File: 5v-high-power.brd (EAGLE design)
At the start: 92.7 x 34.6 mm, 31 parts, among them IC1 LM2576, J1 Bypass, J2 En, J3 12v, J4 5V Out, J5 LEN EN, J6 POWERPOLE_POWER25A, J7 POWERPOLE_POWER25A, Q1 SI4532ADY

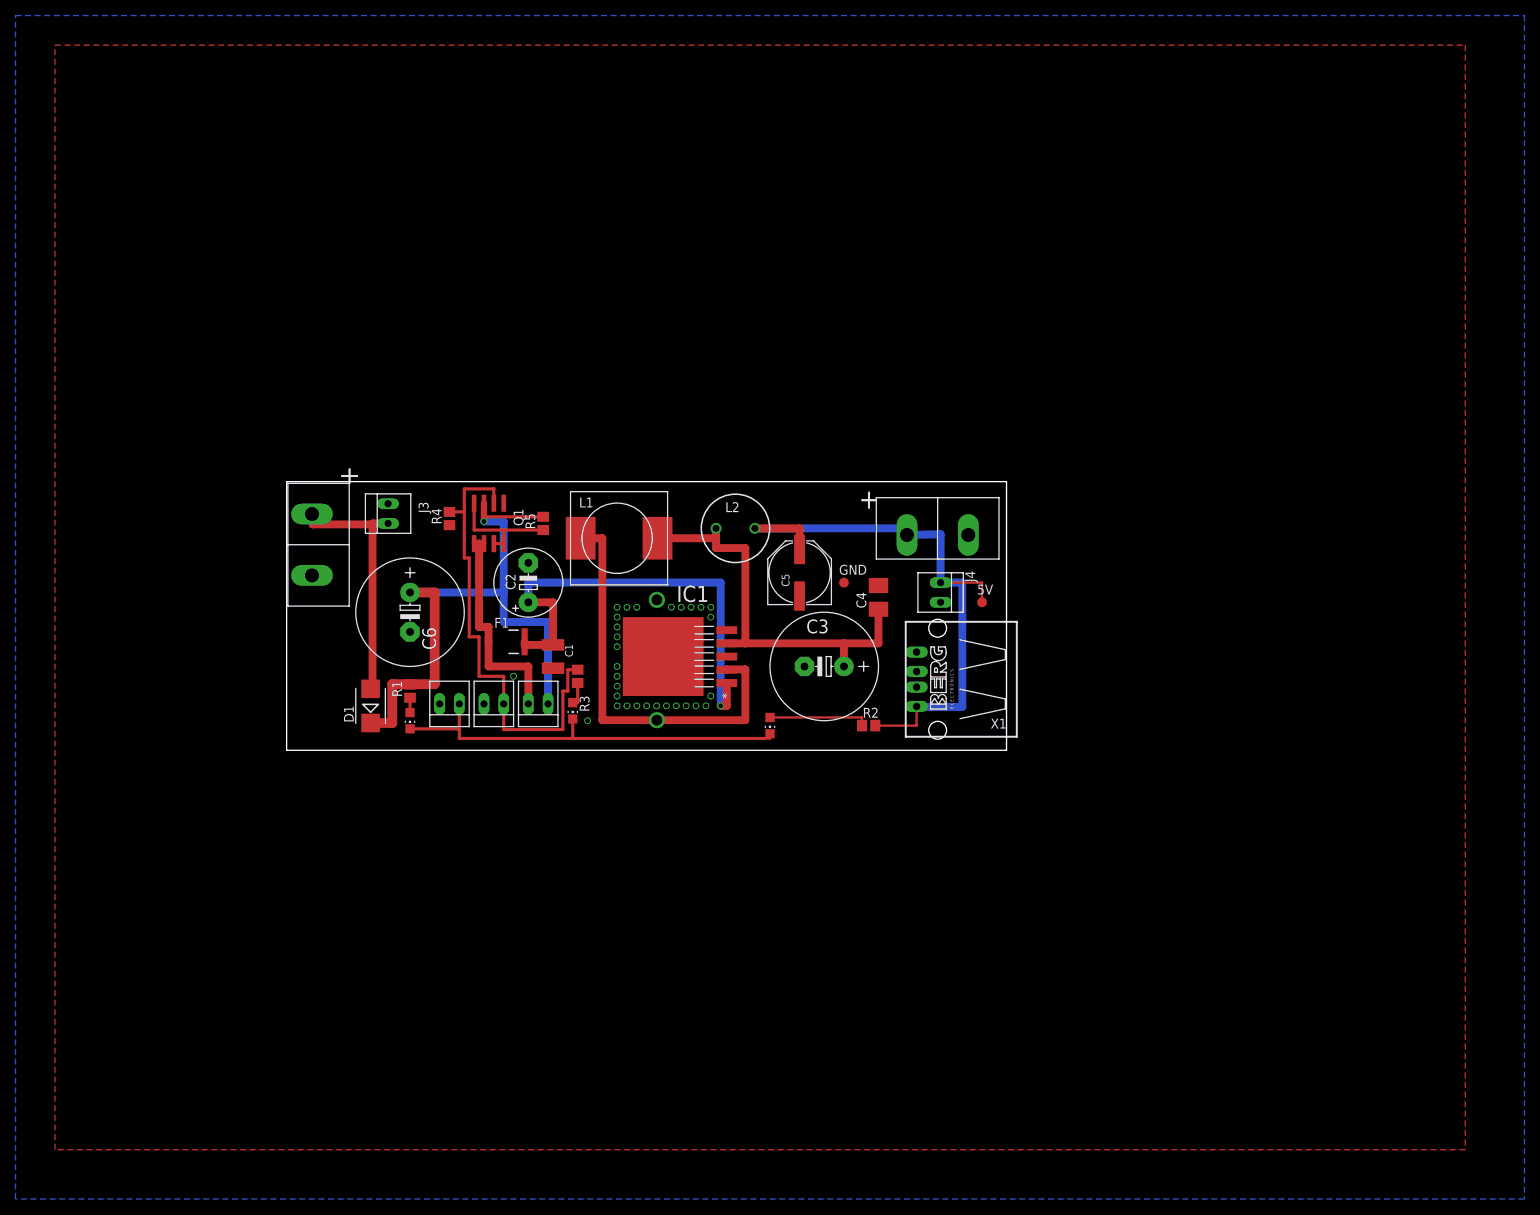
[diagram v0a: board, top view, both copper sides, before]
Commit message: uses a4 frame and smaller ground plane area to make printing better
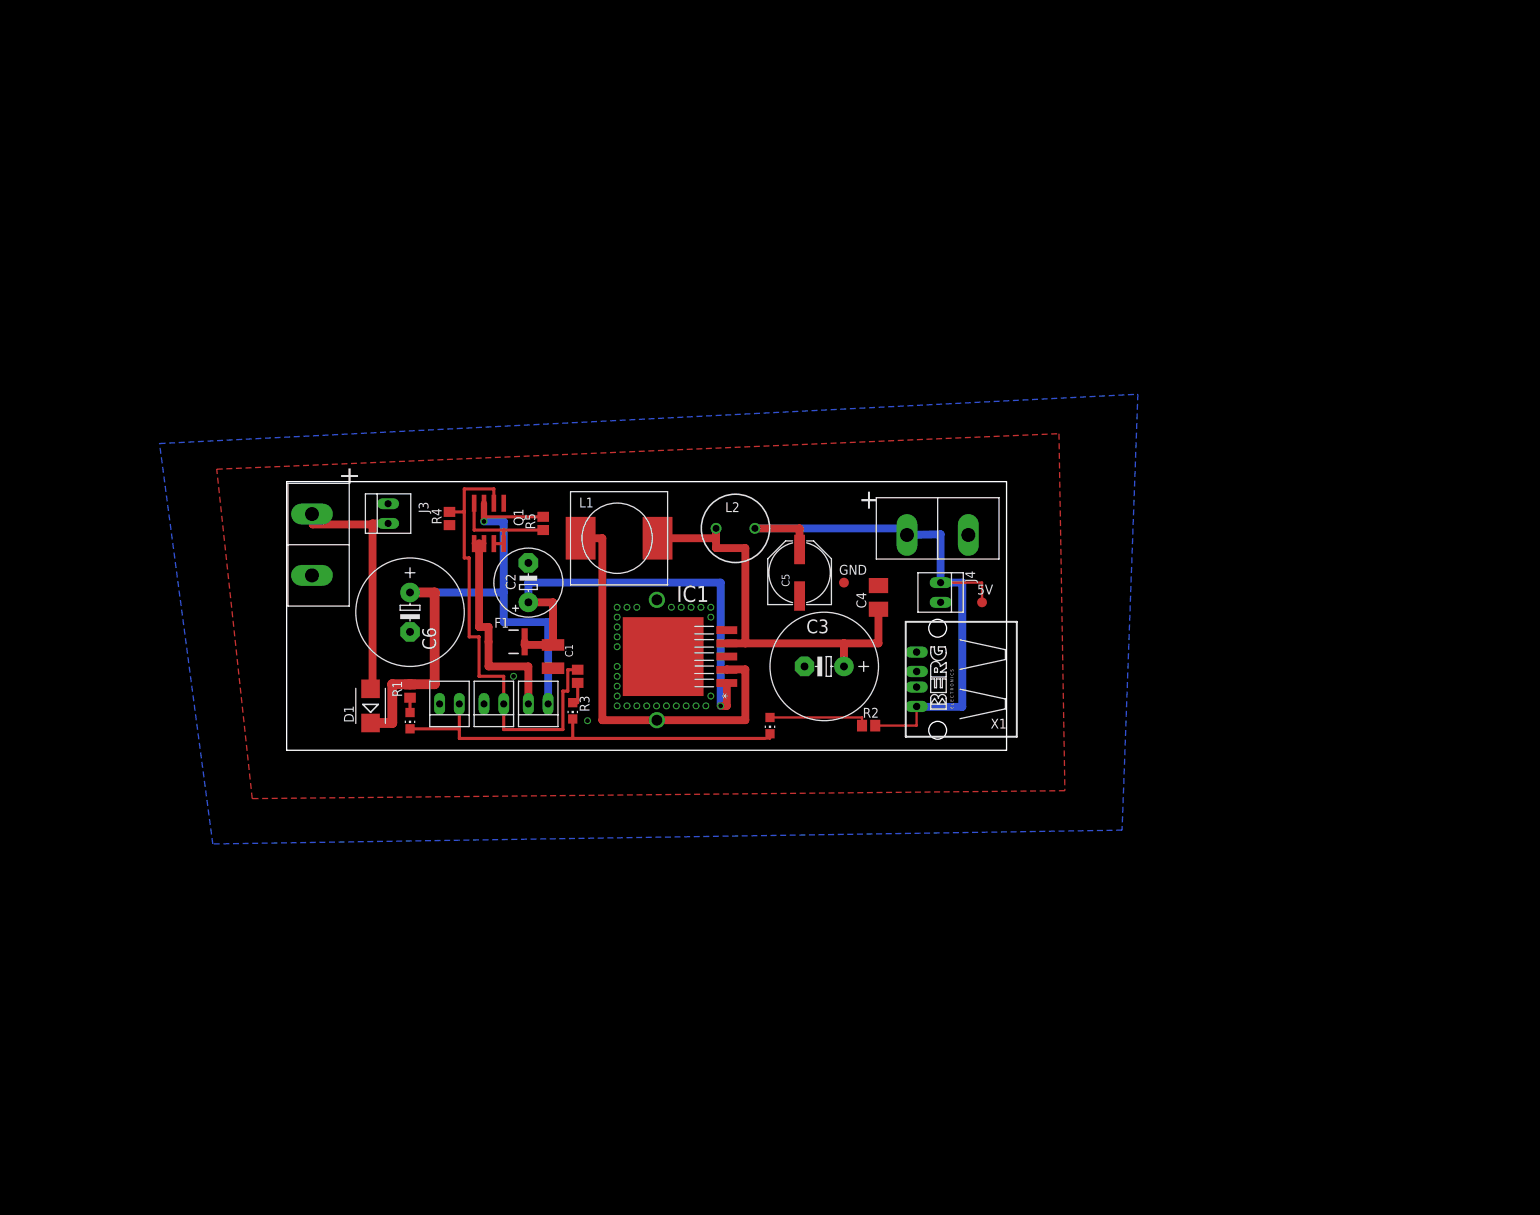
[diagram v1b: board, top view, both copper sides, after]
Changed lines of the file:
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@@
 <contactref element="C6" pad="-"/>
 <polygon width="1.016" layer="16">
-<vertex x="-12.7" y="127"/>
-<vertex x="181.61" y="127"/>
-<vertex x="181.61" y="-25.4"/>
-<vertex x="-12.7" y="-25.4"/>
+<vertex x="5.842" y="71.882"/>
+<vertex x="131.826" y="78.232"/>
+<vertex x="129.794" y="22.098"/>
+<vertex x="12.7" y="20.32"/>
 </polygon>
 <polygon width="1.016" layer="1">
-<vertex x="-7.62" y="123.19"/>
-<vertex x="173.99" y="123.19"/>
-<vertex x="173.99" y="-19.05"/>
-<vertex x="-7.62" y="-19.05"/>
+<vertex x="13.208" y="68.58"/>
+<vertex x="121.666" y="73.152"/>
+<vertex x="122.428" y="27.178"/>
+<vertex x="17.78" y="26.162"/>
 </polygon>
 <contactref element="GND" pad="TP"/>
